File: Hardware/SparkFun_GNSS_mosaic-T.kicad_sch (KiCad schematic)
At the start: 54 parts, among them J1 microSD, SW1 DPDT_Slide_SMD_7.2x3.5mm, SW2 SMD_5.2x5.2mm_h2.5mm, U1 mosaic-T, U2 74LVC2T45DC

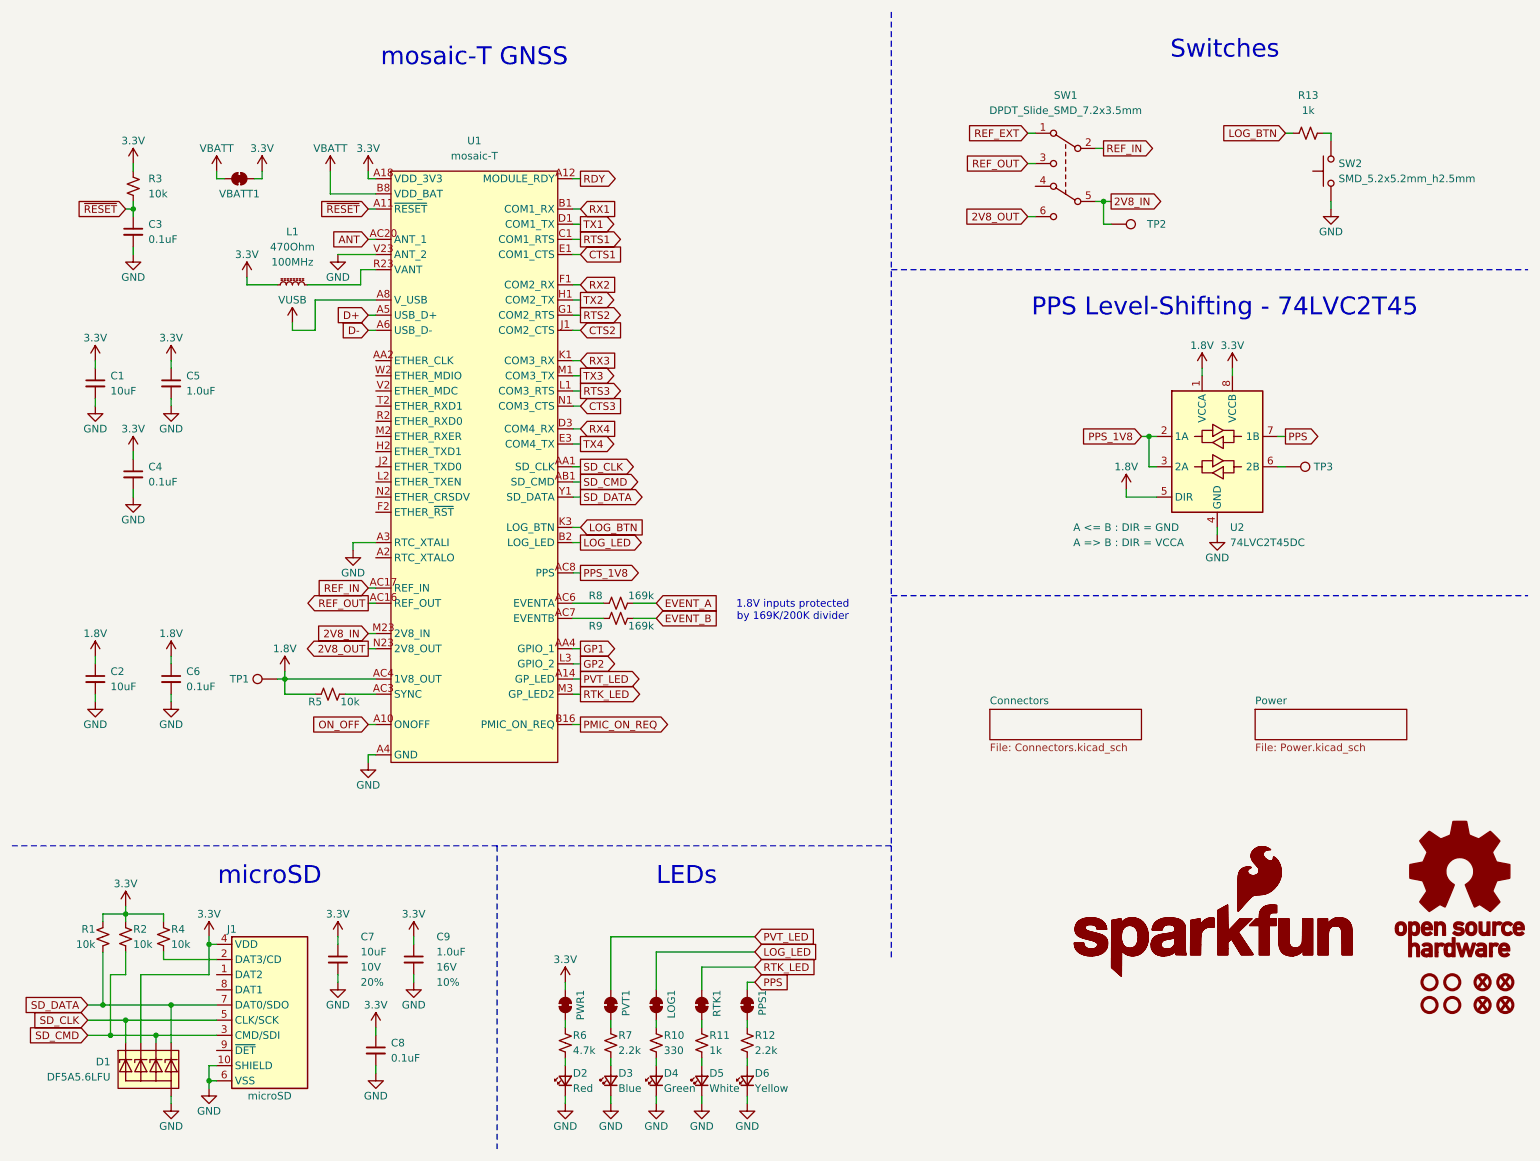
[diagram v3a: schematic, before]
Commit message: Schematic updates after proto review
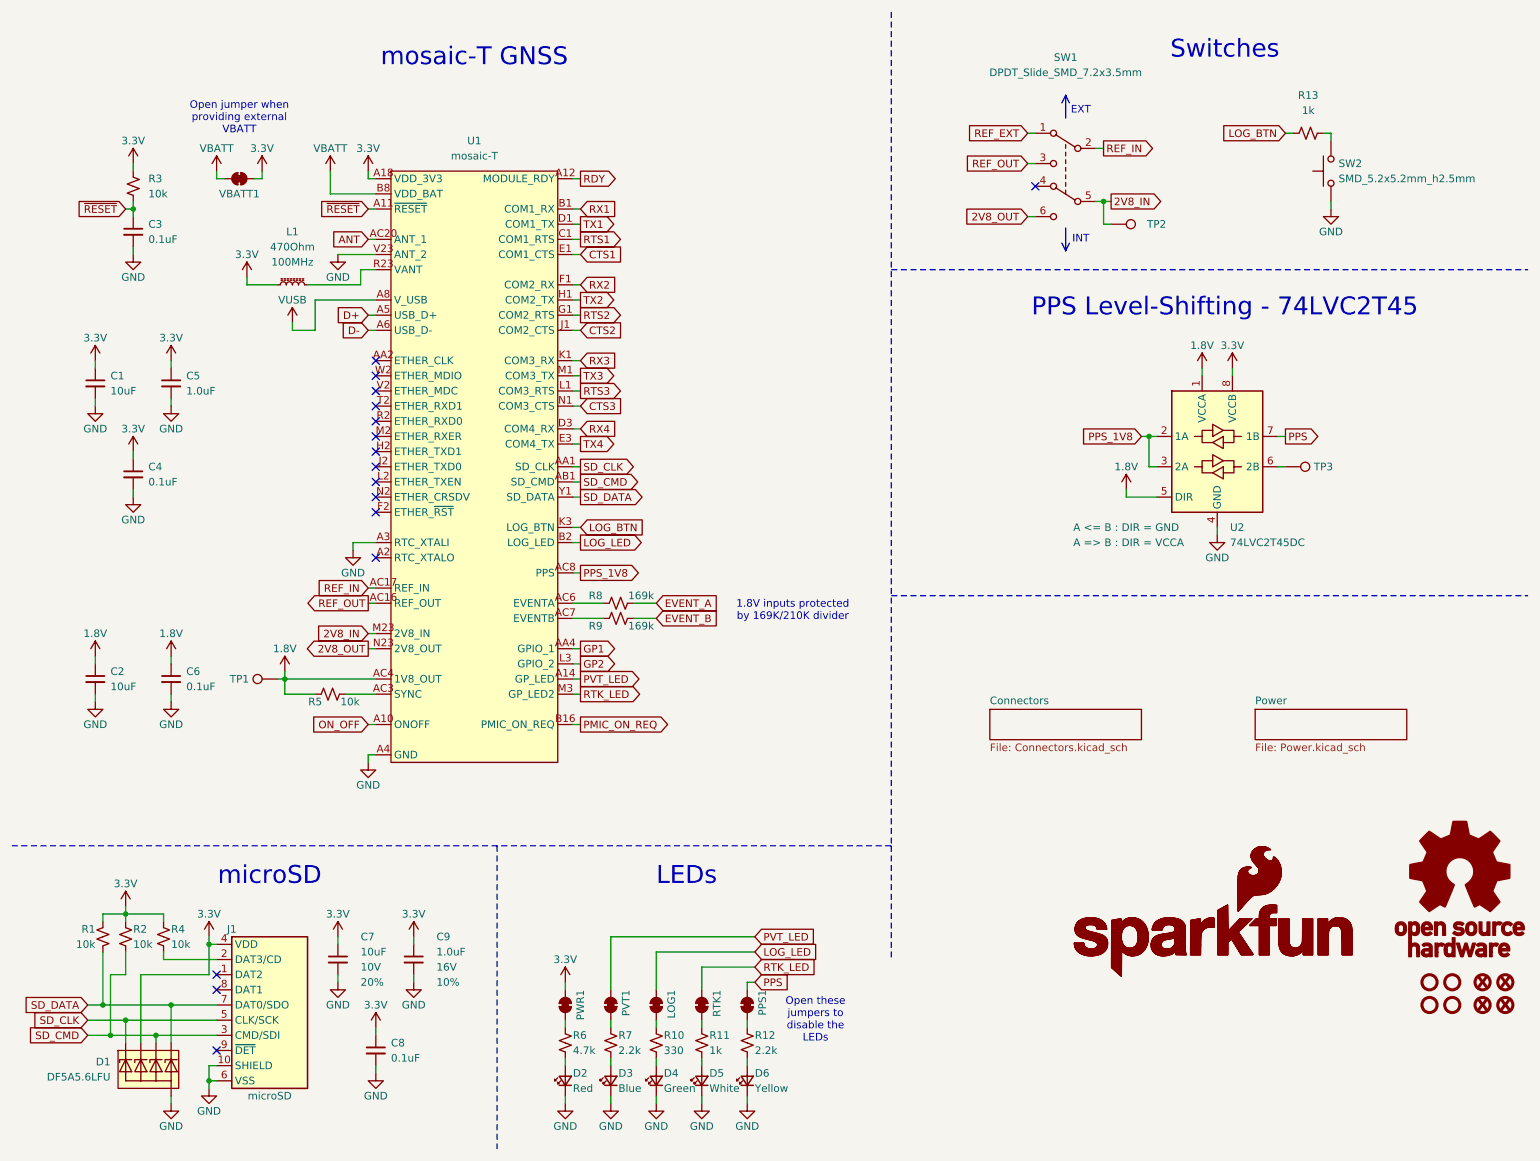
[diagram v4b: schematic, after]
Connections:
- no-connect marks 0 -> 16
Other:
- note added: "1.8V inputs protected by 169K/210K divider"
- note added: "EXT"
- note added: "INT"
- note added: "Open jumper when providing external VBATT"
- note added: "Open these jumpers to disable the LEDs"
- note removed: "1.8V inputs protected by 169K/200K divider"
- company: SparkFun -> SparkFun Electronics
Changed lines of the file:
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@@
 	(title_block
 		(title "SparkFun GNSS mosaic-T")
-		(date "2025-03-13")
+		(date "2025-03-19")
 		(rev "v01")
-		(company "SparkFun")
+		(company "SparkFun Electronics")
 		(comment 1 "Designed by: P.C.")
 	)
@@
 		)
 	)
+	(text "Open jumper when\nproviding external\nVBATT"
+		(exclude_from_sim no)
+		(at 50.8 30.48 0)
+		(effects
+			(font
+				(size 1.27 1.27)
+			)
+		)
+	)
 	(text "mosaic-T GNSS"
 		(exclude_from_sim no)
@@
 		)
 	)
+	(text "Open these\njumpers to\ndisable the\nLEDs"
+		(exclude_from_sim no)
+		(at 147.32 181.61 0)
+		(effects
+			(font
+				(size 1.27 1.27)
+			)
+		)
+	)
 	(text "microSD"
 		(exclude_from_sim no)
@@
 		)
 	)
-	(text "1.8V inputs protected\nby 169K/200K divider"
+	(text "EXT"
+		(exclude_from_sim no)
+		(at 191.77 29.21 0)
+		(effects
+			(font
+				(size 1.27 1.27)
+			)
+		)
+	)
+	(text "1.8V inputs protected\nby 169K/210K divider"
 		(exclude_from_sim no)
 		(at 143.51 113.03 0)
@@
 		)
 	)
+	(text "INT"
+		(exclude_from_sim no)
+		(at 191.77 50.8 0)
+		(effects
+			(font
+				(size 1.27 1.27)
+			)
+		)
+	)
 	(junction
 		(at 203.2 83.82)
@@
 		(color 0 0 0 0)
 	)
+	(no_connect
+		(at 73.66 93.98)
+	)
+	(no_connect
+		(at 73.66 91.44)
+	)
+	(no_connect
+		(at 46.99 176.53)
+	)
+	(no_connect
+		(at 73.66 73.66)
+	)
+	(no_connect
+		(at 73.66 104.14)
+	)
+	(no_connect
+		(at 73.66 81.28)
+	)
+	(no_connect
+		(at 73.66 83.82)
+	)
+	(no_connect
+		(at 73.66 88.9)
+	)
+	(no_connect
+		(at 46.99 186.69)
+	)
+	(no_connect
+		(at 73.66 76.2)
+	)
+	(no_connect
+		(at 46.99 173.99)
+	)
+	(no_connect
+		(at 73.66 96.52)
+	)
+	(no_connect
+		(at 73.66 71.12)
+	)
+	(no_connect
+		(at 73.66 78.74)
+	)
+	(no_connect
+		(at 73.66 86.36)
+	)
+	(no_connect
+		(at 184.15 41.91)
+	)
 	(wire
 		(pts
@@
 		)
 	)
+	(polyline
+		(pts
+			(xy 188.595 27.94) (xy 189.23 26.67)
+		)
+		(stroke
+			(width 0)
+			(type default)
+		)
+	)
 	(wire
 		(pts
@@
 		)
 	)
+	(polyline
+		(pts
+			(xy 189.23 26.67) (xy 189.23 30.48)
+		)
+		(stroke
+			(width 0)
+			(type default)
+		)
+	)
 	(wire
 		(pts
@@
 		)
 	)
+	(polyline
+		(pts
+			(xy 188.595 51.435) (xy 189.23 52.705)
+		)
+		(stroke
+			(width 0)
+			(type default)
+		)
+	)
 	(wire
 		(pts
@@
 		)
 	)
+	(polyline
+		(pts
+			(xy 189.23 52.705) (xy 189.865 51.435)
+		)
+		(stroke
+			(width 0)
+			(type default)
+		)
+	)
 	(wire
 		(pts
@@
 		)
 	)
+	(polyline
+		(pts
+			(xy 189.23 26.67) (xy 189.865 27.94)
+		)
+		(stroke
+			(width 0)
+			(type default)
+		)
+	)
 	(wire
 		(pts
@@
 		)
 	)
+	(polyline
+		(pts
+			(xy 189.23 52.705) (xy 189.23 48.895)
+		)
+		(stroke
+			(width 0)
+			(type default)
+		)
+	)
 	(wire
 		(pts
@@
 		(dnp no)
 		(property "Reference" "SW1"
-			(at 189.23 26.67 0)
+			(at 189.23 20.32 0)
 			(effects
 				(font
@@
 		)
 		(property "Value" "DPDT_Slide_SMD_7.2x3.5mm"
-			(at 189.23 29.21 0)
+			(at 189.23 22.86 0)
 			(effects
 				(font

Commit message: More updates, post proto review
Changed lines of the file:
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@@
-		(color 0 0 0 0)
-	)
-	(junction
-		(at 29.21 184.15)
-		(diameter 0)
 		(color 0 0 0 0)
 	)
@@
 	(wire
 		(pts
-			(xy 31.75 170.18) (xy 31.75 173.99)
-		)
-		(stroke
-			(width 0)
-			(type default)
-		)
-	)
-	(wire
-		(pts
 			(xy 45.72 168.91) (xy 45.72 167.64)
 		)
@@
 	(wire
 		(pts
-			(xy 31.75 173.99) (xy 29.21 173.99)
-		)
-		(stroke
-			(width 0)
-			(type default)
-		)
-	)
-	(wire
-		(pts
 			(xy 34.29 173.99) (xy 45.72 173.99)
 		)
@@
 	(wire
 		(pts
+			(xy 31.75 176.53) (xy 36.83 176.53)
+		)
+		(stroke
+			(width 0)
+			(type default)
+		)
+	)
+	(wire
+		(pts
 			(xy 72.39 137.16) (xy 72.39 138.43)
 		)
@@
 	(wire
 		(pts
+			(xy 31.75 170.18) (xy 31.75 176.53)
+		)
+		(stroke
+			(width 0)
+			(type default)
+		)
+	)
+	(wire
+		(pts
 			(xy 45.72 168.91) (xy 46.99 168.91)
 		)
@@
 	(wire
 		(pts
-			(xy 29.21 184.15) (xy 36.83 184.15)
+			(xy 25.4 184.15) (xy 36.83 184.15)
 		)
 		(stroke
@@
 	(wire
 		(pts
-			(xy 25.4 184.15) (xy 29.21 184.15)
-		)
-		(stroke
-			(width 0)
-			(type default)
-		)
-	)
-	(wire
-		(pts
 			(xy 72.39 50.8) (xy 73.66 50.8)
 		)
@@
 		(pts
 			(xy 120.65 187.96) (xy 120.65 189.23)
+		)
+		(stroke
+			(width 0)
+			(type default)
+		)
+	)
+	(wire
+		(pts
+			(xy 36.83 176.53) (xy 36.83 184.15)
 		)
 		(stroke
@@
 		)
 		(stroke
-			(width 0)
-			(type default)
-		)
-	)
-	(wire
-		(pts
-			(xy 29.21 173.99) (xy 29.21 184.15)
-		)
-		(stroke
